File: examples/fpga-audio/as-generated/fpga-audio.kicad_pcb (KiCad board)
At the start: 2 copper layers, 100 x 84 mm, 29 parts, among them J1 3V3 IN, J2 AUDIO OUT, J3 SPI PROG, U1 iCE40UP5K, U2 PCM5102A, U3 AP2112K-1.2, U4 W25Q32JV, X1 12MHz

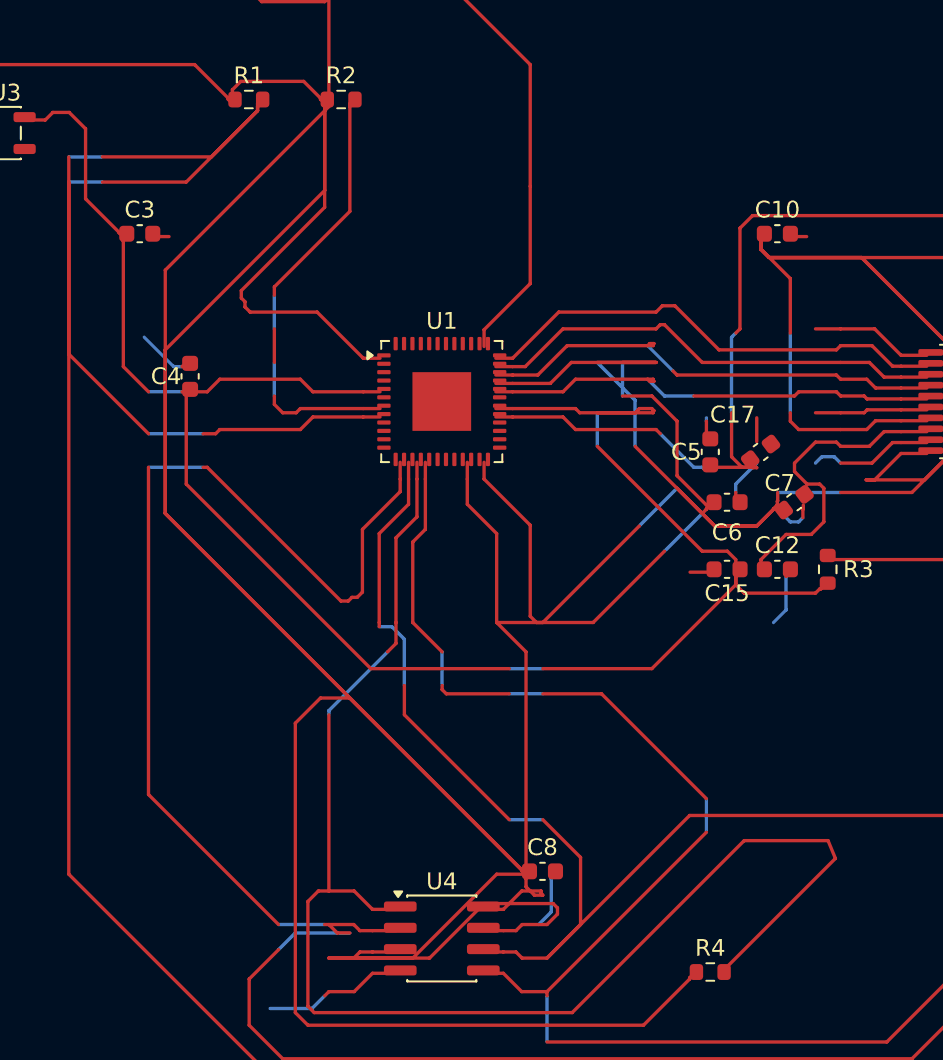
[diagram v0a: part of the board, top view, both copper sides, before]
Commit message: Measure the copper that goes out and comes back, and the text drawn on text
The reviewer sent screenshots with circles on them. Two kinds: strings
printed through each other on the schematics, and copper that leaves a
pad, travels three sides of a rectangle and arrives four millimetres
away. Neither had a rule that could see it - `text_over_wire` measured
text against nets and nothing measured text against text, and
`route.detour` weighs a whole net, which averages one bad connection
away under any ratio worth setting.

New rule `route.wander`: one continuous run of copper - pad or junction
at each end - against the shortest way between those two ends that
clears the packages in between. The baseline walks the perimeter of
whatever the straight line crosses, so an opamp's feedback wrap is
measured against going round the package rather than through it. On
KiCad's 18 demo boards it fires once at the shipped 2.0x.

`readability.text_over_text` and `_over_wire` are regraded info: they
fire on 14 and 10 of those 18 human sheets. That is the estimate
talking, not the drawing. `ai-generated` still promotes both to errors,
so every generated design has to have none - and the five examples do.

What the two rules then made us fix:

* a net label's anchor cannot move, but its reading direction can. Each
  name is now offered the four quarters of its anchor and takes the
  first that prints over nothing. Power symbol names and PWR_FLAG names
  get the same treatment - four grounds on one row printed GNGNGNGND.
  Schematic text overlaps: buck 1, motor 2, carrier 1, fpga 7, all to 0.
* a plane crossing was priced at forty times front copper per
  millimetre, which is a prohibition, not a price: one millimetre of
  crossing bought a forty millimetre tour and the boards had grown
  them. Thirty is where neither `route.wander` nor `route.return_path`
  fires. Buck, motor and carrier now have no wander findings.
* `write_variant` resolves the routes a second time, so the
  straight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
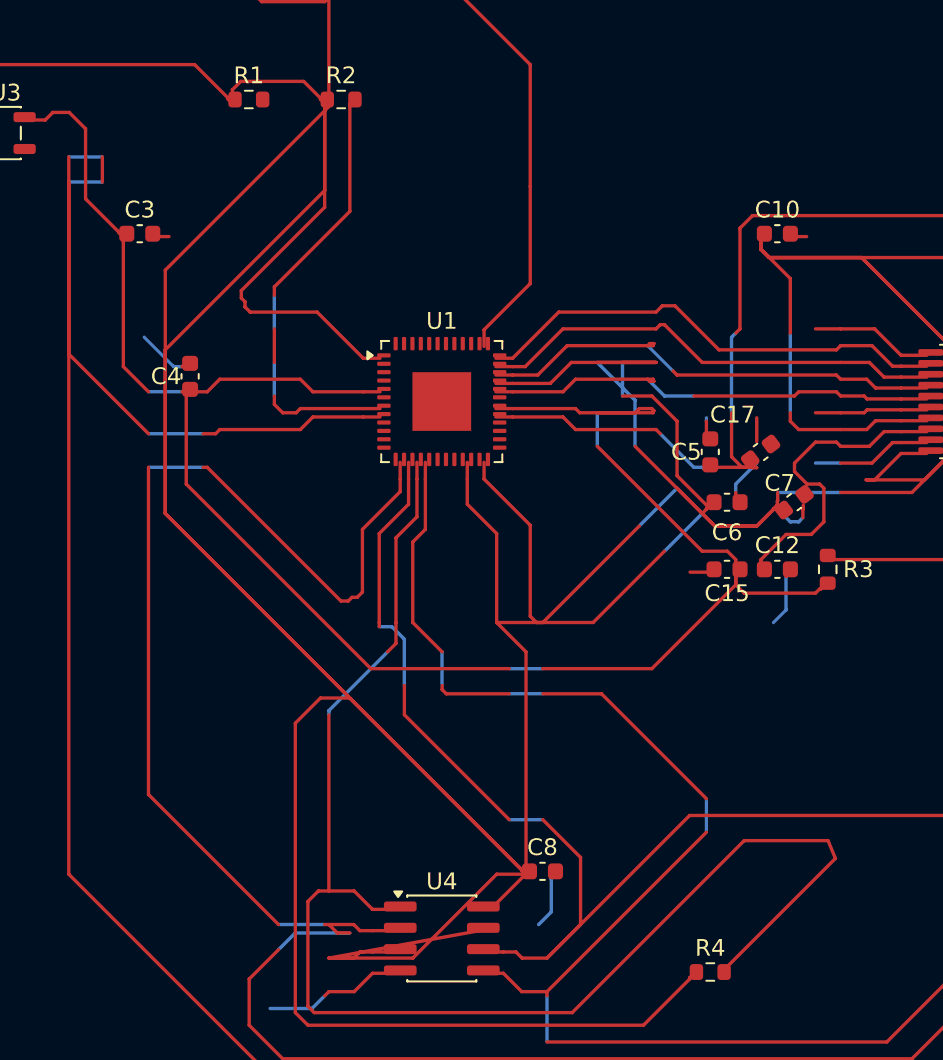
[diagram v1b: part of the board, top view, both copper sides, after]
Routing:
- net /CRESET: track 162.7 -> 141.8 mm
- net +3V3: track 629.1 -> 615.0 mm
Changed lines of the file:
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@@
 	(segment (start 135.005 135.0) (end 133.5 135.0) (width 0.2) (layer "F.Cu") (net 1))
 	(segment (start 133.5 135.0) (end 133.25 135.25) (width 0.2) (layer "F.Cu") (net 1))
-	(segment (start 142.475 130.095) (end 143.9 130.095) (width 0.2) (layer "F.Cu") (net 3))
-	(segment (start 143.9 130.095) (end 144.995 129.0) (width 0.2) (layer "F.Cu") (net 3))
-	(segment (start 144.995 129.0) (end 146.146 129.0) (width 0.2) (layer "F.Cu") (net 3))
-	(segment (start 146.146 129.0) (end 146.146 129.146) (width 0.2) (layer "F.Cu") (net 3))
-	(segment (start 146.146 129.146) (end 146.25 129.25) (width 0.2) (layer "F.Cu") (net 3))
-	(segment (start 146.25 129.25) (end 145.75 129.25) (width 0.2) (layer "F.Cu") (net 3))
-	(segment (start 145.75 129.25) (end 145.25 128.75) (width 0.2) (layer "F.Cu") (net 3))
-	(segment (start 145.25 128.75) (end 145.25 128.25) (width 0.2) (layer "F.Cu") (net 3))
-	(segment (start 145.25 128.25) (end 145.225 128.225) (width 0.2) (layer "F.Cu") (net 3))
-	(segment (start 145.225 128.225) (end 145.225 128.0) (width 0.2) (layer "F.Cu") (net 3))
-	(segment (start 142.475 131.365) (end 143.9 131.365) (width 0.2) (layer "F.Cu") (net 3))
-	(segment (start 143.9 131.365) (end 144.65 131.365) (width 0.2) (layer "F.Cu") (net 3))
-	(segment (start 144.65 131.365) (end 145.015 131.0) (width 0.2) (layer "F.Cu") (net 3))
-	(segment (start 145.015 131.0) (end 146.5 131.0) (width 0.2) (layer "F.Cu") (net 3))
-	(segment (start 146.5 131.0) (end 147.125 130.375) (width 0.2) (layer "F.Cu") (net 3))
-	(segment (start 147.125 130.375) (end 147.125 130.009) (width 0.2) (layer "F.Cu") (net 3))
-	(segment (start 147.125 130.009) (end 146.866 129.75) (width 0.2) (layer "F.Cu") (net 3))
-	(segment (start 146.866 129.75) (end 142.75 129.75) (width 0.2) (layer "F.Cu") (net 3))
-	(segment (start 142.75 129.75) (end 139.5 133.0) (width 0.2) (layer "F.Cu") (net 3))
-	(segment (start 139.5 133.0) (end 133.5 133.0) (width 0.2) (layer "F.Cu") (net 3))
+	(segment (start 142.475 130.095) (end 143.13 130.095) (width 0.2) (layer "F.Cu") (net 3))
+	(segment (start 143.13 130.095) (end 145.225 128.0) (width 0.2) (layer "F.Cu") (net 3))
+	(segment (start 142.475 131.365) (end 133.5 133.0) (width 0.2) (layer "F.Cu") (net 3))
 	(segment (start 142.475 132.635) (end 143.9 132.635) (width 0.2) (layer "F.Cu") (net 16))
 	(segment (start 143.9 132.635) (end 144.65 132.635) (width 0.2) (layer "F.Cu") (net 16))
@@
 	(segment (start 118.0 97.0) (end 118.0 86.75) (width 0.2) (layer "F.Cu") (net 8))
 	(segment (start 118.0 86.75) (end 120.0 86.75) (width 0.2) (layer "B.Cu") (net 8))
-	(segment (start 120.0 86.75) (end 125.0 86.75) (width 0.2) (layer "F.Cu") (net 8))
-	(segment (start 125.0 86.75) (end 129.25 82.5) (width 0.2) (layer "F.Cu") (net 8))
-	(segment (start 129.25 82.5) (end 129.25 82.25) (width 0.2) (layer "F.Cu") (net 8))
-	(segment (start 129.25 82.25) (end 129.25 82.075) (width 0.2) (layer "F.Cu") (net 8))
-	(segment (start 129.25 82.075) (end 129.325 82.0) (width 0.2) (layer "F.Cu") (net 8))
-	(segment (start 129.325 82.0) (end 129.325 82.175) (width 0.2) (layer "F.Cu") (net 8))
-	(segment (start 129.325 82.175) (end 129.25 82.25) (width 0.2) (layer "F.Cu") (net 8))
-	(segment (start 129.25 82.25) (end 129.25 82.5) (width 0.2) (layer "F.Cu") (net 8))
-	(segment (start 129.25 82.5) (end 126.5 85.25) (width 0.2) (layer "F.Cu") (net 8))
-	(segment (start 126.5 85.25) (end 120.0 85.25) (width 0.2) (layer "F.Cu") (net 8))
+	(segment (start 120.0 86.75) (end 120.0 85.25) (width 0.2) (layer "F.Cu") (net 8))
 	(segment (start 120.0 85.25) (end 118.0 85.25) (width 0.2) (layer "B.Cu") (net 8))
 	(segment (start 118.0 85.25) (end 118.0 128.0) (width 0.2) (layer "F.Cu") (net 8))
@@
 	(segment (start 133.25 135.25) (end 132.5 136.0) (width 0.2) (layer "B.Cu") (net 1))
 	(segment (start 132.5 136.0) (end 130.0 136.0) (width 0.2) (layer "B.Cu") (net 1))
-	(segment (start 164.0 103.5) (end 163.625 103.125) (width 0.2) (layer "B.Cu") (net 1))
-	(segment (start 163.625 103.125) (end 162.875 103.125) (width 0.2) (layer "B.Cu") (net 1))
-	(segment (start 162.875 103.125) (end 162.5 103.5) (width 0.2) (layer "B.Cu") (net 1))
+	(segment (start 164.0 103.5) (end 162.5 103.5) (width 0.2) (layer "B.Cu") (net 1))
 	(segment (start 182.5 95.5) (end 184.0 95.5) (width 0.2) (layer "B.Cu") (net 1))
 	(segment (start 184.0 95.5) (end 186.0 93.5) (width 0.2) (layer "B.Cu") (net 1))

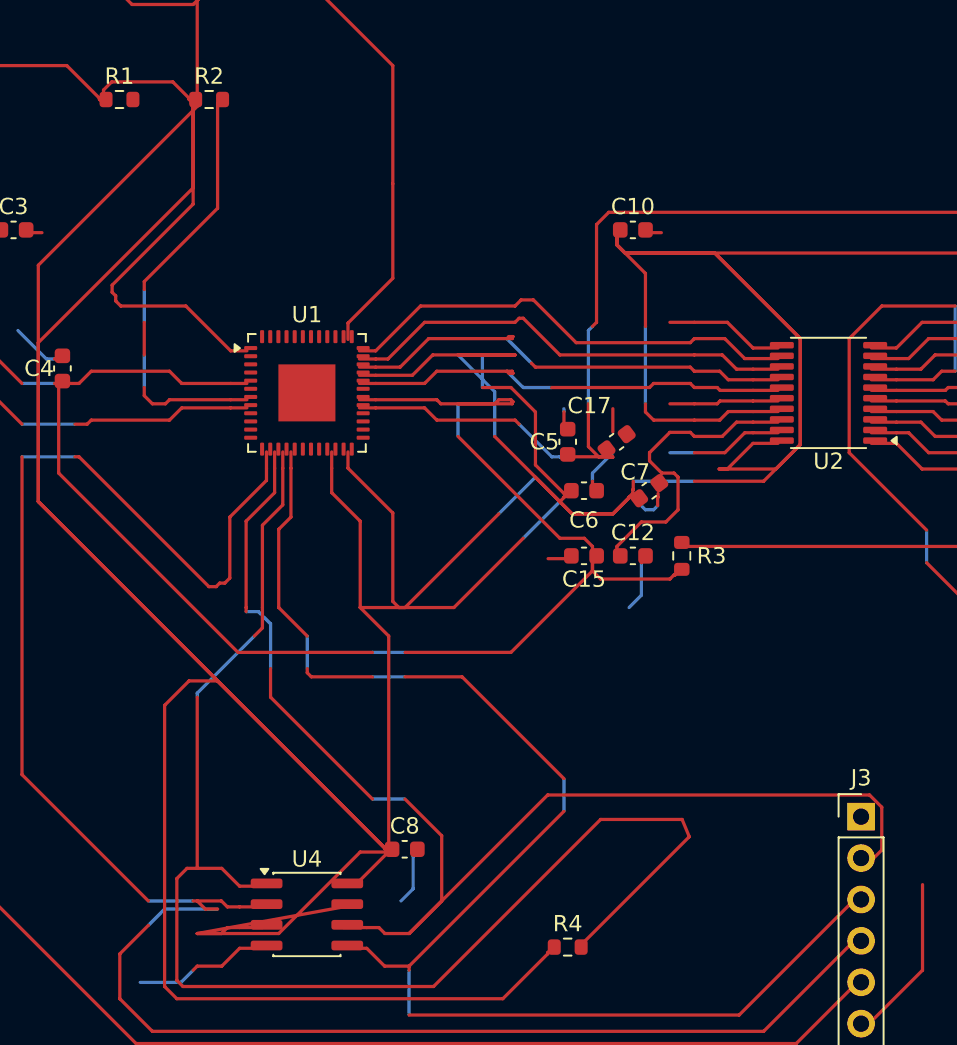
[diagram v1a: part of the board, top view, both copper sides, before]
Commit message: Stop hiding the hairpins behind the pads they are drawn on
The reviewer said the 135 degree bends and the odd-angle runs were still
there. They were. `route.acute_angle` skipped any corner within a pad's
*radius*, and a 0805's radius is 0.47 mm, which covers the five or six
ordinary corners a chamfered pad entry leaves inside it. Eleven of the
thirteen hairpins on these five boards sat in that shadow, because a pad
is exactly where a route that has to double back does it.

The exemption is the pad's connection point now, not a disc around it.
Two branches leaving one pad stay exempt - the pad's own copper fills the
wedge, so it is not an acid trap - but nought degrees never is: that is
one run drawn twice, and no pad excuses it.

Then the generator had to stop making them:

* `_untraced` drops the copper a second run lays on top of the first.
  The shorter is inside the longer and carries nothing it does not; both
  get trimmed, because dropping only the duplicate leaves the other
  hanging over the gap, which is `route.stub`. It runs before the runs
  are joined, while the pair is still two tracks sharing an end - once
  joined, the shared point is usually a pad, and the clean-up passes pin
  those precisely so they cannot take copper off them.
* `_straighten` only takes the direct line when it lands on the 45 grid.
  Between two pads at whatever coordinates their packages give them it
  usually does not: last round it made a nine millimetre run at 169.7
  degrees, which is the slip-of-the-mouse angle `route.odd_angle` is for.

Measured across the five boards: off-grid segments 1 to 0, 180 degree
reversals 6 to 0, and the motor board's `route.return_path` finding went
with the 11 mm of copper it was measuring.

Three corners survive, all on the FPGA board, all where a knee lands a
fraction past where its own two legs cross - legs of 0.07 and 0.25 mm on
two, 0.15 and 0.5 mm on the third. Refusing a knee that short is worse:
the segment then keeps the angle it had, a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
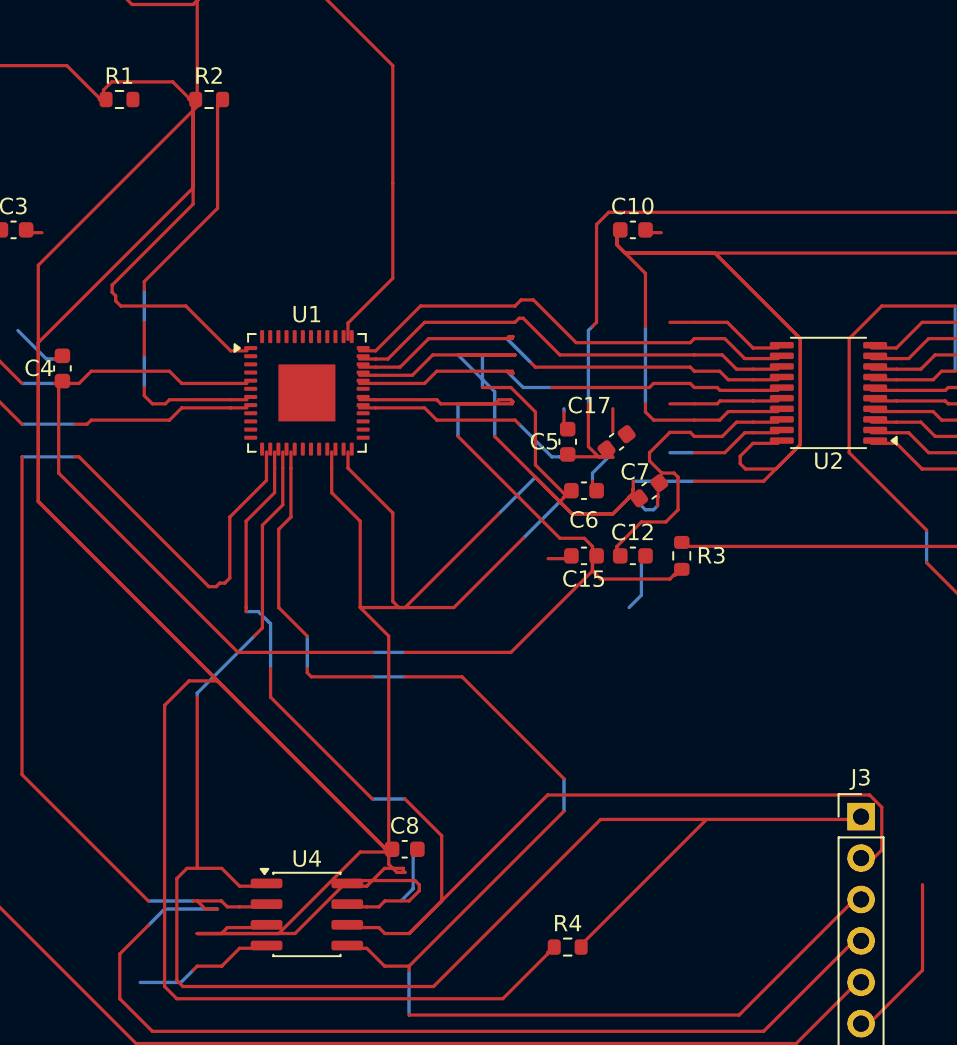
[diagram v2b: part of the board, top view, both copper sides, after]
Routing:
- net +3V3: track 615.0 -> 626.7 mm
- net /SPI_SS: track 86.3 -> 97.4 mm
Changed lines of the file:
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@@
 	(segment (start 165.8688 103.5) (end 164.0 103.5) (width 0.2) (layer "F.Cu") (net 1))
 	(segment (start 169.1375 102.925) (end 167.6 102.925) (width 0.2) (layer "F.Cu") (net 3))
-	(segment (start 167.6 102.925) (end 166.025 104.5) (width 0.2) (layer "F.Cu") (net 3))
-	(segment (start 166.025 104.5) (end 165.519 104.5) (width 0.2) (layer "F.Cu") (net 3))
-	(segment (start 165.519 104.5) (end 169.0 104.5) (width 0.2) (layer "F.Cu") (net 3))
+	(segment (start 167.6 102.925) (end 166.812 103.712) (width 0.2) (layer "F.Cu") (net 3))
+	(segment (start 166.812 103.712) (end 166.812 104.173) (width 0.2) (layer "F.Cu") (net 3))
+	(segment (start 166.812 104.173) (end 167.139 104.5) (width 0.2) (layer "F.Cu") (net 3))
+	(segment (start 167.139 104.5) (end 169.0 104.5) (width 0.2) (layer "F.Cu") (net 3))
 	(segment (start 169.0 104.5) (end 170.5 103.0) (width 0.2) (layer "F.Cu") (net 3))
 	(segment (start 170.5 103.0) (end 170.5 96.5) (width 0.2) (layer "F.Cu") (net 3))
@@
 	(segment (start 135.005 135.0) (end 133.5 135.0) (width 0.2) (layer "F.Cu") (net 1))
 	(segment (start 133.5 135.0) (end 133.25 135.25) (width 0.2) (layer "F.Cu") (net 1))
-	(segment (start 142.475 130.095) (end 143.13 130.095) (width 0.2) (layer "F.Cu") (net 3))
-	(segment (start 143.13 130.095) (end 145.225 128.0) (width 0.2) (layer "F.Cu") (net 3))
-	(segment (start 142.475 131.365) (end 133.5 133.0) (width 0.2) (layer "F.Cu") (net 3))
+	(segment (start 142.475 130.095) (end 143.9 130.095) (width 0.2) (layer "F.Cu") (net 3))
+	(segment (start 143.9 130.095) (end 144.995 129.0) (width 0.2) (layer "F.Cu") (net 3))
+	(segment (start 144.995 129.0) (end 146.146 129.0) (width 0.2) (layer "F.Cu") (net 3))
+	(segment (start 146.146 129.0) (end 146.146 129.146) (width 0.2) (layer "F.Cu") (net 3))
+	(segment (start 146.146 129.146) (end 146.25 129.25) (width 0.2) (layer "F.Cu") (net 3))
+	(segment (start 146.25 129.25) (end 145.75 129.25) (width 0.2) (layer "F.Cu") (net 3))
+	(segment (start 145.75 129.25) (end 145.25 128.75) (width 0.2) (layer "F.Cu") (net 3))
+	(segment (start 145.25 128.75) (end 145.25 128.25) (width 0.2) (layer "F.Cu") (net 3))
+	(segment (start 145.25 128.25) (end 145.225 128.225) (width 0.2) (layer "F.Cu") (net 3))
+	(segment (start 145.225 128.225) (end 145.225 128.0) (width 0.2) (layer "F.Cu") (net 3))
+	(segment (start 142.475 131.365) (end 143.9 131.365) (width 0.2) (layer "F.Cu") (net 3))
+	(segment (start 143.9 131.365) (end 144.65 131.365) (width 0.2) (layer "F.Cu") (net 3))
+	(segment (start 144.65 131.365) (end 145.015 131.0) (width 0.2) (layer "F.Cu") (net 3))
+	(segment (start 145.015 131.0) (end 146.5 131.0) (width 0.2) (layer "F.Cu") (net 3))
+	(segment (start 146.5 131.0) (end 147.125 130.375) (width 0.2) (layer "F.Cu") (net 3))
+	(segment (start 147.125 130.375) (end 147.125 130.009) (width 0.2) (layer "F.Cu") (net 3))
+	(segment (start 147.125 130.009) (end 146.866 129.75) (width 0.2) (layer "F.Cu") (net 3))
+	(segment (start 146.866 129.75) (end 142.75 129.75) (width 0.2) (layer "F.Cu") (net 3))
+	(segment (start 142.75 129.75) (end 139.5 133.0) (width 0.2) (layer "F.Cu") (net 3))
+	(segment (start 139.5 133.0) (end 133.5 133.0) (width 0.2) (layer "F.Cu") (net 3))
 	(segment (start 142.475 132.635) (end 143.9 132.635) (width 0.2) (layer "F.Cu") (net 16))
 	(segment (start 143.9 132.635) (end 144.65 132.635) (width 0.2) (layer "F.Cu") (net 16))
@@
 	(segment (start 125.5 79.75) (end 127.5 81.75) (width 0.2) (layer "F.Cu") (net 3))
 	(segment (start 127.5 81.75) (end 127.5 81.825) (width 0.2) (layer "F.Cu") (net 3))
-	(segment (start 127.5 81.825) (end 127.675 82.0) (width 0.2) (layer "F.Cu") (net 3))
-	(segment (start 127.675 82.0) (end 127.675 81.825) (width 0.2) (layer "F.Cu") (net 3))
+	(segment (start 127.5 81.825) (end 127.5875 81.9125) (width 0.2) (layer "F.Cu") (net 3))
+	(segment (start 127.5875 81.9125) (end 127.675 81.825) (width 0.2) (layer "F.Cu") (net 3))
 	(segment (start 127.675 81.825) (end 127.75 81.75) (width 0.2) (layer "F.Cu") (net 3))
 	(segment (start 127.75 81.75) (end 127.75 81.25) (width 0.2) (layer "F.Cu") (net 3))
@@
 	(segment (start 132.625 136.25) (end 148.0 136.25) (width 0.2) (layer "F.Cu") (net 19))
 	(segment (start 148.0 136.25) (end 158.25 126.0) (width 0.2) (layer "F.Cu") (net 19))
-	(segment (start 158.25 126.0) (end 163.25 126.0) (width 0.2) (layer "F.Cu") (net 19))
-	(segment (start 163.25 126.0) (end 163.689 127.061) (width 0.2) (layer "F.Cu") (net 19))
-	(segment (start 163.689 127.061) (end 157.0 133.75) (width 0.2) (layer "F.Cu") (net 19))
+	(segment (start 158.25 126.0) (end 174.0 126.0) (width 0.2) (layer "F.Cu") (net 19))
+	(segment (start 164.75 126.0) (end 157.0 133.75) (width 0.2) (layer "F.Cu") (net 19))
 	(segment (start 157.0 133.75) (end 157.0 133.825) (width 0.2) (layer "F.Cu") (net 19))
 	(segment (start 157.0 133.825) (end 156.825 134.0) (width 0.2) (layer "F.Cu") (net 19))
